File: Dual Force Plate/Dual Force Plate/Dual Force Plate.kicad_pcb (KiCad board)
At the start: 2 copper layers, 140 x 80 mm, 26 parts, among them J10 Conn_01x07_Pin, J3 Conn_01x07_Pin, J4 Conn_01x07_Pin, J6 Conn_01x02_Pin, J7 Conn_01x04_Pin, J8 Conn_01x02_Pin, J9 Conn_01x07_Pin, SW1 SW_SPST, U1 MT3608, U2 ESP32-DevKitC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

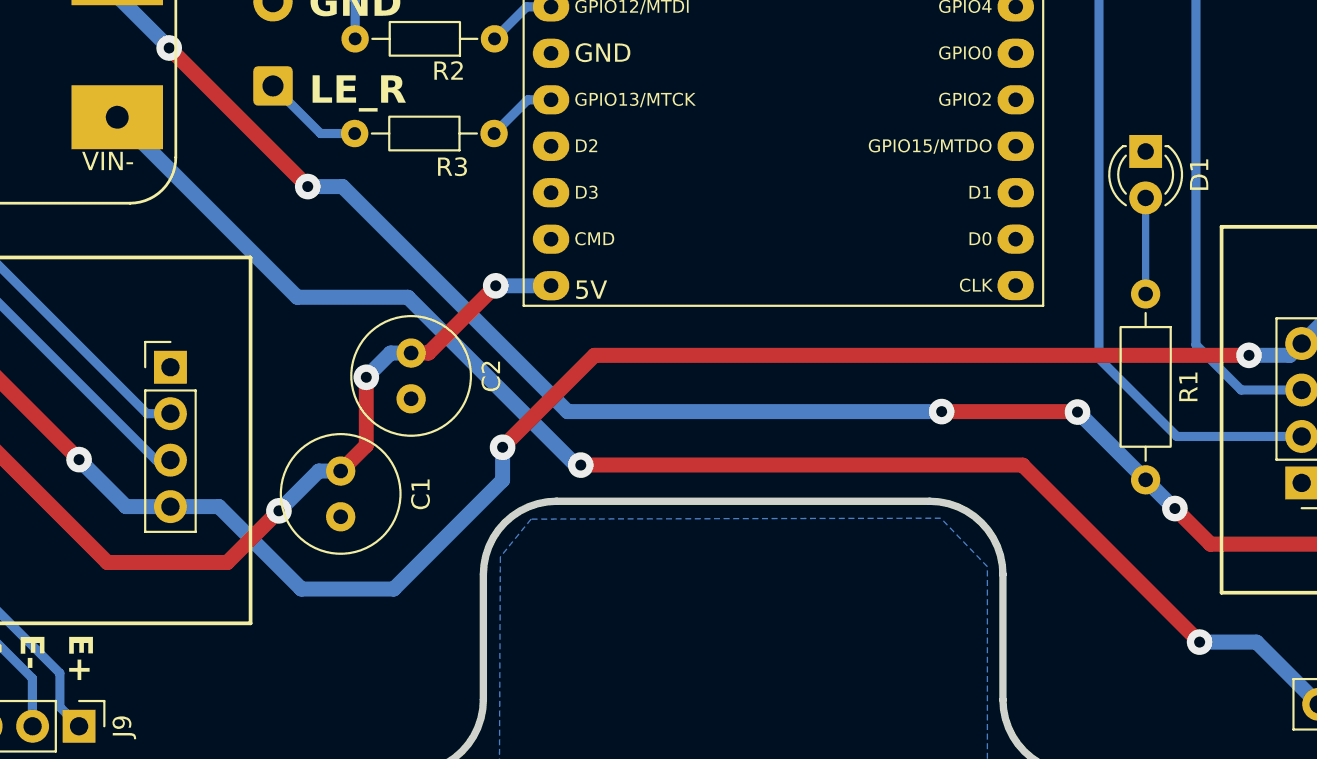
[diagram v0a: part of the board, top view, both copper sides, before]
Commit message: Edit the Layout of (DUAL_FORCE_PLATE)
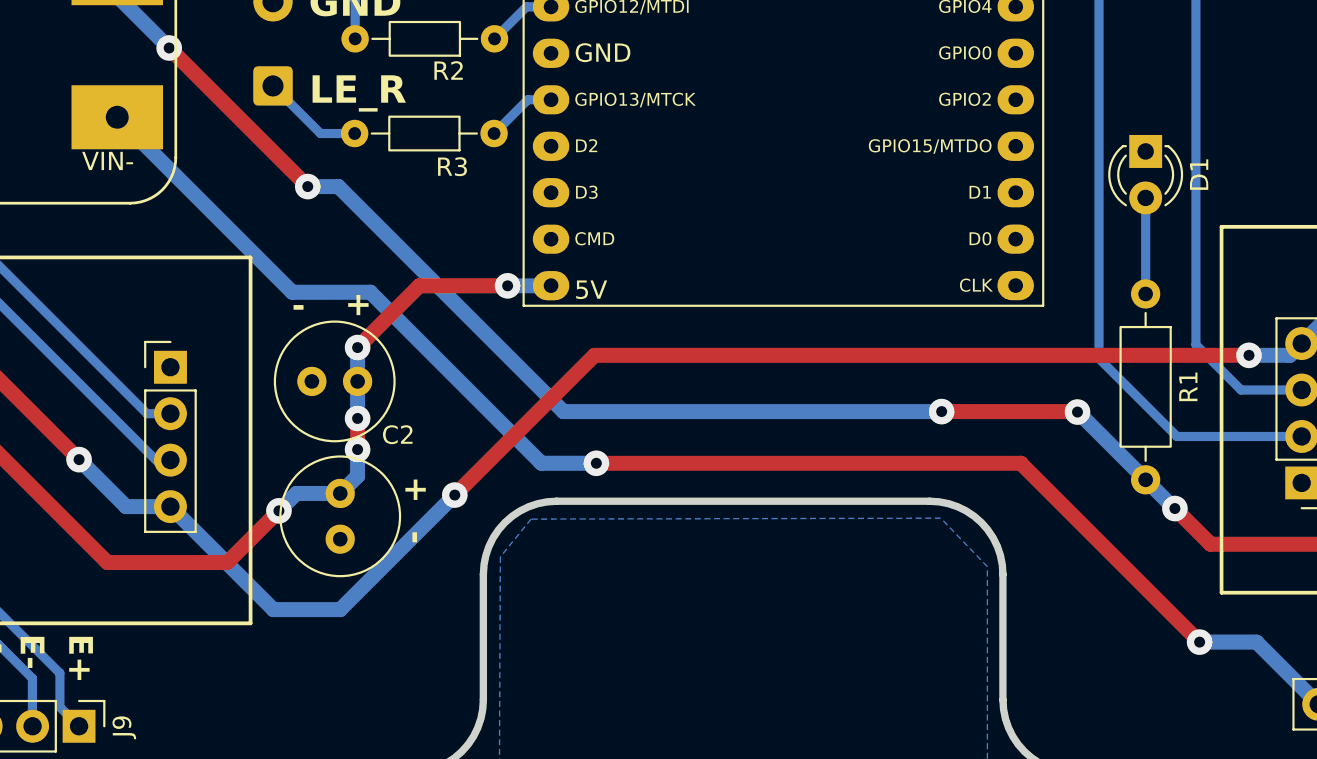
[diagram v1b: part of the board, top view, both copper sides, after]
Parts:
- moved C2 3.31 mm to (141.9, 128.3), turned to 180 degrees
- moved C1 1.23 mm to (141.0, 134.5)
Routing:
- net +5V: track 77.4 -> 79.4 mm, vias 4 -> 6
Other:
- board text added: "+"
- board text added: "-"
